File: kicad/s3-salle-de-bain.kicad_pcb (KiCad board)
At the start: 2 copper layers, 76.7 x 108 mm, 27 parts, among them J1 Jack-3.5mm, J2 USB-C, Q1 AO3401, Q2 AO3401, SW1 EC11, SW2 Mute-SPDT, U1 ESP32-S3-DevKitC-1, U2 GY-PCM5102, U3 PAM8403, U4 INMP441, U5 AMS1117-3.3

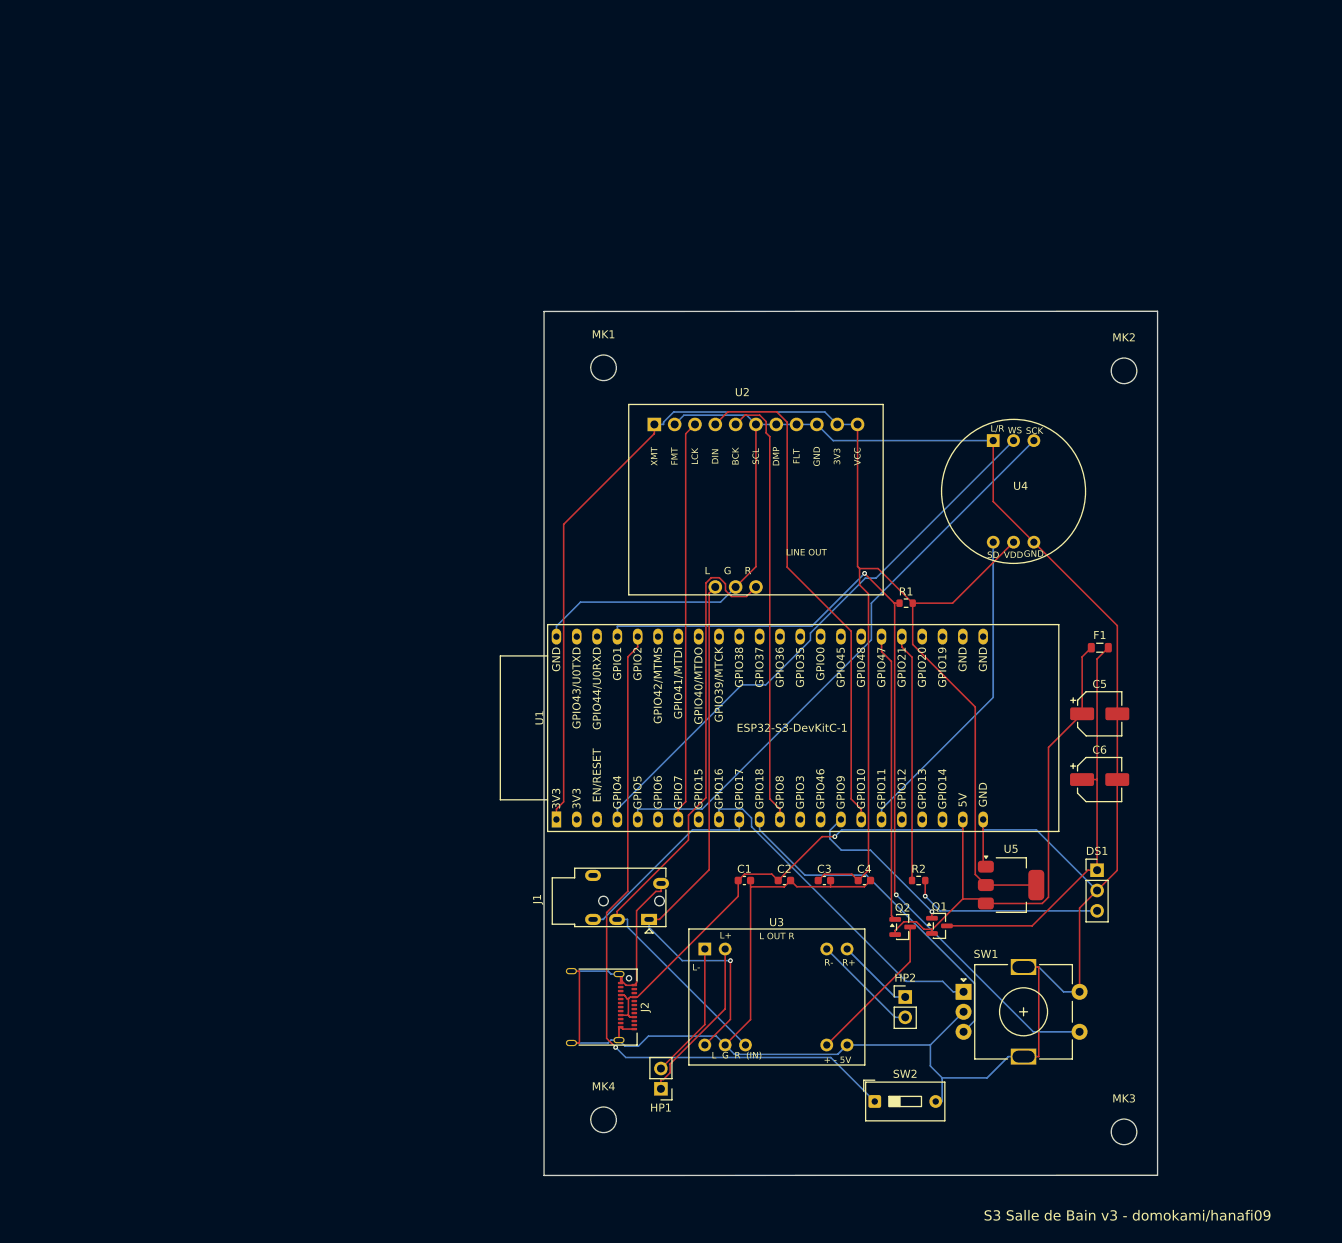
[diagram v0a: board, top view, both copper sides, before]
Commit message: feat: ampli externe 4 voies (LOTHYE) -> 4 HP ACTIFS
L'utilisateur passe a un ampli 4 voies (2x PAM8403). Le PAM8403 est 2 voies :
la carte "4 voies" = 2x PAM8403. Source stereo dupliquee sur 4 HP actifs.

PCB:
- retire le PAM8403 soude (U3) + les 2 connecteurs HP embarques
- ajoute J3 (alim 5V de l'ampli externe, gated par Q2/GPIO47)
- l'audio sort par le jack 3.5mm J1 (deja cable AUDIO_L/R) -> entree ampli
- DRC: 0 violation ; rendu PCB regenere

Docs (DOCX + PDF):
- boitier v6 : 4 HP ACTIFS (2 facade + 2 bouts), plus de radiateurs passifs
- ampli externe 4 voies decrit ; Fig. 2 (PCB) mise a jour

Co-Authored-By: Claude Opus 4.8 <noreply@anthropic.com>
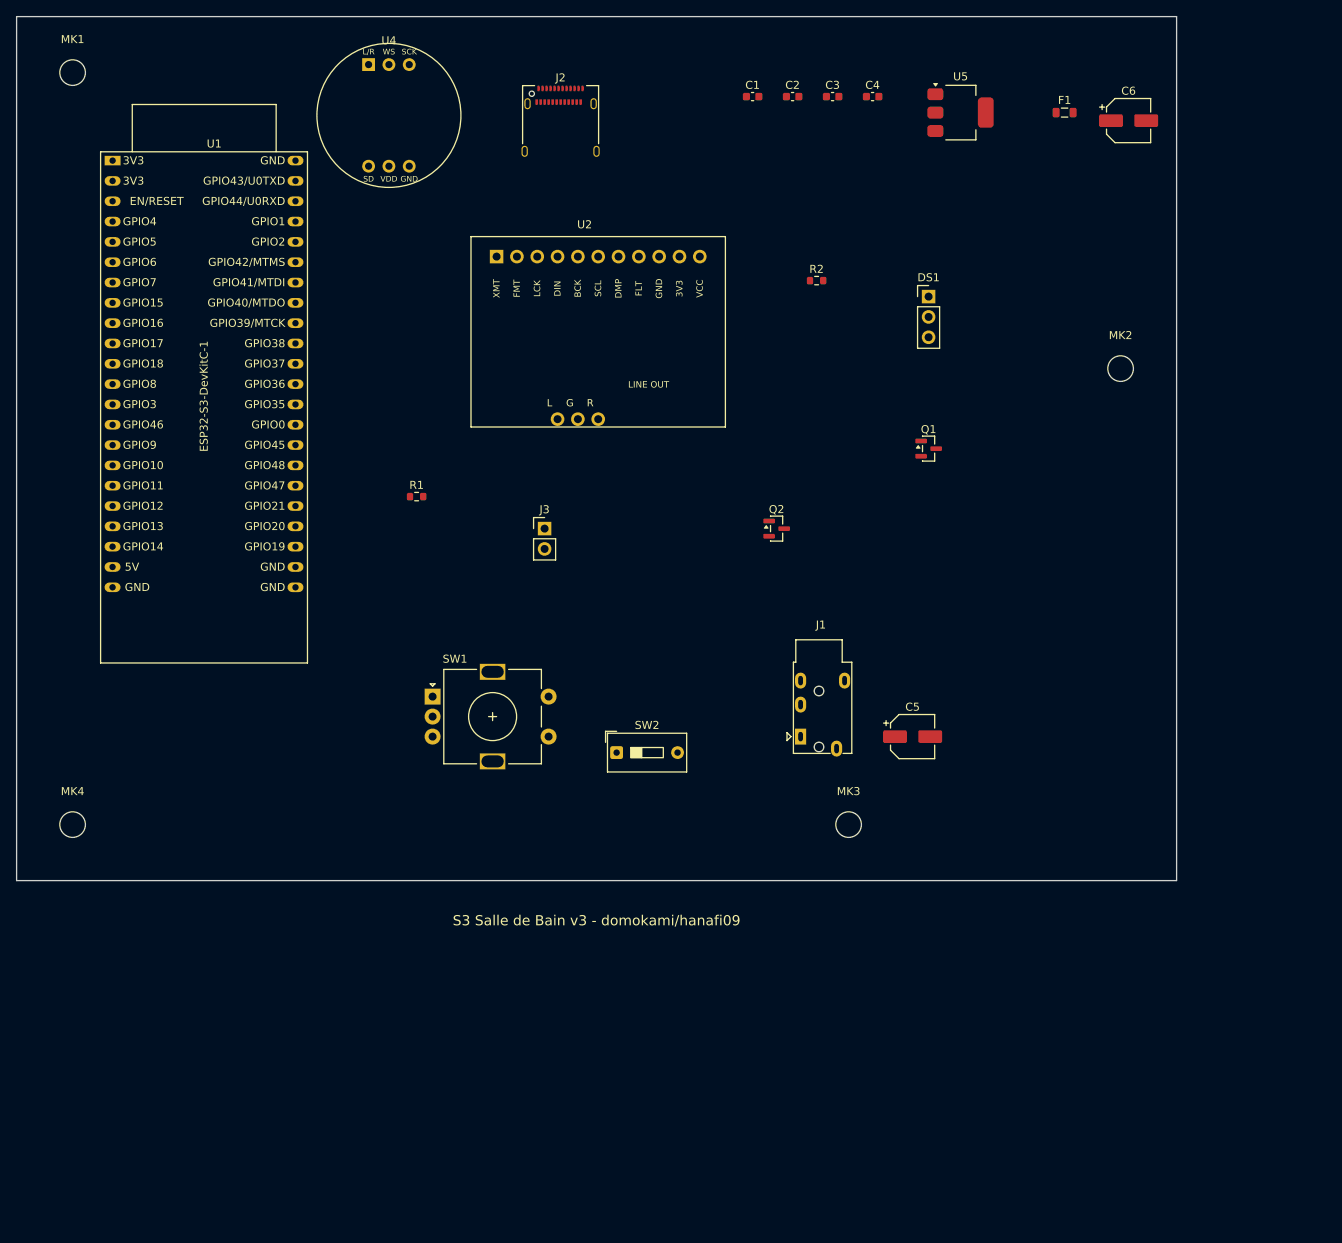
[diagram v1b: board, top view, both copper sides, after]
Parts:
- removed HP1: HP-Left, PinHeader_1x02_P2.54mm_Vertical
- removed HP2: HP-Right, PinHeader_1x02_P2.54mm_Vertical
- removed U3: PAM8403, PAM8403-mini
- added J3: AMP-5V, PinHeader_1x02_P2.54mm_Vertical, F.Cu at (66.0, 64.0)
- moved J2 109.9 mm to (68.0, 14.0), turned to 0 degrees
- moved U1 99.3 mm to (12.0, 18.0), turned to 0 degrees
- moved C1 98.0 mm to (92.0, 10.0)
- moved C2 98.0 mm to (97.0, 10.0)
- moved C3 98.0 mm to (102.0, 10.0)
- moved C4 98.0 mm to (107.0, 10.0)
- moved U5 96.8 mm to (118.0, 12.0)
- moved U4 91.1 mm to (44.0, 6.00)
- moved C6 82.4 mm to (139.0, 13.0)
- moved R2 76.1 mm to (100.0, 33.0)
- moved MK1 75.9 mm to (7.00, 7.00)
- moved MK4 75.9 mm to (7.00, 101.0)
- moved SW1 75.9 mm to (52.0, 85.0)
- moved DS1 74.7 mm to (114.0, 35.0)
- moved F1 67.0 mm to (131.0, 12.0)
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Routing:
- net GND: track 364.6 -> 0.00 mm
- net +3V3: track 214.6 -> 0.00 mm
- net +5V: track 125.2 -> 0.00 mm, vias 1 -> 0
- net BTN_CENTER: track 107.4 -> 0.00 mm, vias 2 -> 0
- net MUTE_SW: track 88.6 -> 0.00 mm, vias 1 -> 0
- net AUDIO_R: track 78.2 -> 0.00 mm
- net MIC_BCLK: track 72.6 -> 0.00 mm
- net AUDIO_L: track 70.5 -> 0.00 mm, vias 1 -> 0
- net MIC_LRCLK: track 70.4 -> 0.00 mm
- net DAC_DIN: track 63.7 -> 0.00 mm
- net DAC_BCK: track 55.1 -> 0.00 mm
- net +5V_LED: track 51.9 -> 0.00 mm
- net DAC_LRCK: track 50.2 -> 0.00 mm
- net ENC_B: track 42.7 -> 0.00 mm
- net ENC_A: track 42.0 -> 0.00 mm
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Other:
- board size 76.7 x 108 mm -> 145 x 108 mm

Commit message: revert: retour a l'ancien PCB (PAM8403 soude 2 voies)
Annule la refonte ampli 4 voies (commit 6156e1e) : restaure le PAM8403
soude U3 + connecteurs HP1/HP2, retire J3. Docs (DOCX/PDF) revenues a la
version v6 coherente (2 HP actifs + 2 radiateurs passifs). Fichiers
restaures depuis ac44fe8.

Co-Authored-By: Claude Opus 4.8 <noreply@anthropic.com>
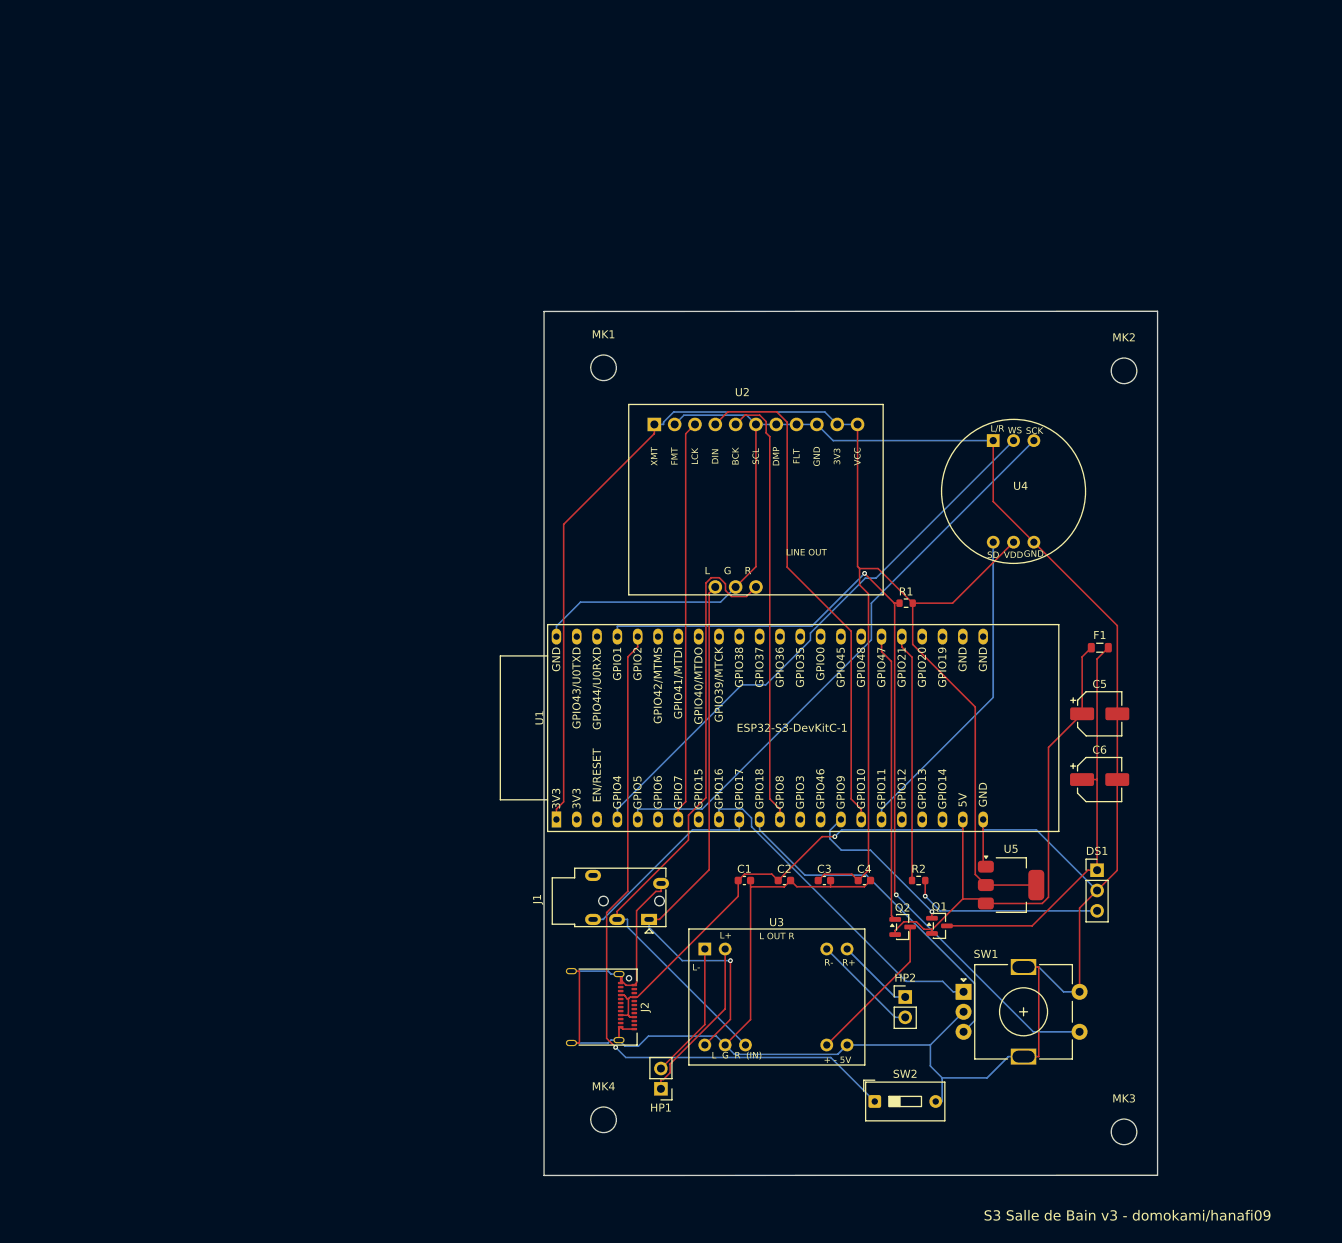
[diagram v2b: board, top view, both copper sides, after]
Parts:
- removed J3: AMP-5V, PinHeader_1x02_P2.54mm_Vertical
- added HP1: HP-Left, PinHeader_1x02_P2.54mm_Vertical, F.Cu at (80.5, 134.0)
- added HP2: HP-Right, PinHeader_1x02_P2.54mm_Vertical, F.Cu at (111.1, 122.5)
- added U3: PAM8403, PAM8403-mini, F.Cu at (86.0, 116.5)
- moved J2 109.9 mm to (72.2, 123.8), turned to -90 degrees
- moved U1 99.3 mm to (67.5, 100.4), turned to 90 degrees
- moved C1 98.0 mm to (91.0, 108.0)
- moved C2 98.0 mm to (96.0, 108.0)
- moved C3 98.0 mm to (101.0, 108.0)
- moved C4 98.0 mm to (106.0, 108.0)
- moved U5 96.8 mm to (124.3, 108.6)
- moved U4 91.1 mm to (122.1, 53.0)
- moved C6 82.4 mm to (135.4, 95.4)
- moved R2 76.1 mm to (112.8, 108.0)
- moved MK1 75.9 mm to (73.4, 43.9)
- moved MK4 75.9 mm to (73.4, 137.9)
- moved SW1 75.9 mm to (118.4, 121.9)
- moved DS1 74.7 mm to (135.1, 106.7)
- moved F1 67.0 mm to (135.4, 78.9)
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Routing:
- net GND: track 0.00 -> 364.6 mm
- net +3V3: track 0.00 -> 214.6 mm
- net +5V: track 0.00 -> 125.2 mm, vias 0 -> 1
- net BTN_CENTER: track 0.00 -> 107.4 mm, vias 0 -> 2
- net MUTE_SW: track 0.00 -> 88.6 mm, vias 0 -> 1
- net AUDIO_R: track 0.00 -> 78.2 mm
- net MIC_BCLK: track 0.00 -> 72.6 mm
- net AUDIO_L: track 0.00 -> 70.5 mm, vias 0 -> 1
- net MIC_LRCLK: track 0.00 -> 70.4 mm
- net DAC_DIN: track 0.00 -> 63.7 mm
- net DAC_BCK: track 0.00 -> 55.1 mm
- net +5V_LED: track 0.00 -> 51.9 mm
- net DAC_LRCK: track 0.00 -> 50.2 mm
- net ENC_B: track 0.00 -> 42.7 mm
- net ENC_A: track 0.00 -> 42.0 mm
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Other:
- board size 145 x 108 mm -> 76.7 x 108 mm
